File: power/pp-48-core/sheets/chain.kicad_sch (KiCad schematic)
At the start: 1 part, among them J301 CHAIN OUT

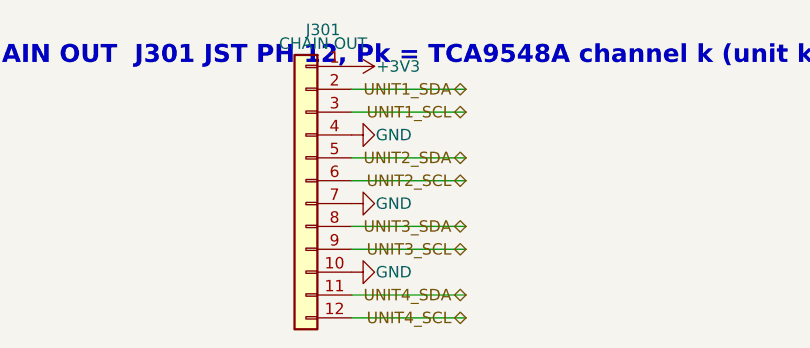
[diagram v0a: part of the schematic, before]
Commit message: pp-48 chained plane: unit board 76 x 72 (9 mm left margin for chain IN J301 + holes, user; slots as rev1 at x 100 / 125; 17 mm input strip with XT60, unit hot-swap, chain OUT J302) and core board 56 x 72 (rev1 core minus the tile, 8 mm right margin for chain OUT J301 + holes, mux U6 by the header, XT30 at the bottom) placed as drafts by tools/place_unit.py / place_core.py (boardfit.py helpers); chain headers on B, pins at v 39..61 on every board; pinout swapped so IN pin 1 = 3V3 / P0 at the bottom on B (flat cable n -> 13 - n); DRC 0 errors besides unconnected, parity clean; not routed; handoff
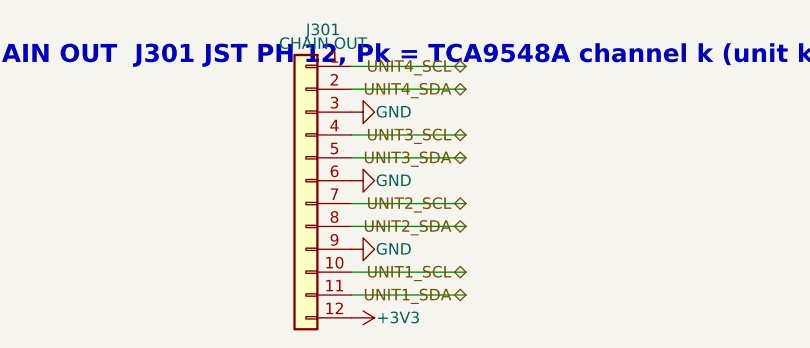
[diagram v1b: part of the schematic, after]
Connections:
- net +3V3: now also J301.12 (Pin_12); no longer J301.1 (Pin_1)
- net GND: now also J301.3 (Pin_3), J301.6 (Pin_6), J301.9 (Pin_9); no longer J301.10 (Pin_10), J301.4 (Pin_4), J301.7 (Pin_7)
- net UNIT1_SCL: now also J301.10 (Pin_10); no longer J301.3 (Pin_3)
- net UNIT1_SDA: now also J301.11 (Pin_11); no longer J301.2 (Pin_2)
- net UNIT2_SCL: now also J301.7 (Pin_7); no longer J301.6 (Pin_6)
- net UNIT2_SDA: now also J301.8 (Pin_8); no longer J301.5 (Pin_5)
- net UNIT3_SCL: now also J301.4 (Pin_4); no longer J301.9 (Pin_9)
- net UNIT3_SDA: now also J301.5 (Pin_5); no longer J301.8 (Pin_8)
- net UNIT4_SCL: now also J301.1 (Pin_1); no longer J301.12 (Pin_12)
- net UNIT4_SDA: now also J301.2 (Pin_2); no longer J301.11 (Pin_11)
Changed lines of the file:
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@@
+	(wire
+		(pts
+			(xy 81.28 38.1) (xy 93.98 38.1)
+		)
+		(stroke
+			(width 0)
+			(type default)
+		)
+	)
 	(wire
 		(pts
@@
 	(wire
 		(pts
-			(xy 81.28 43.18) (xy 93.98 43.18)
+			(xy 81.28 45.72) (xy 93.98 45.72)
 		)
 		(stroke
@@
 	(wire
 		(pts
-			(xy 81.28 50.8) (xy 93.98 50.8)
+			(xy 81.28 53.34) (xy 93.98 53.34)
 		)
 		(stroke
@@
 	(wire
 		(pts
-			(xy 81.28 58.42) (xy 93.98 58.42)
+			(xy 81.28 60.96) (xy 93.98 60.96)
 		)
 		(stroke
@@
 		)
 	)
-	(wire
-		(pts
-			(xy 81.28 66.04) (xy 93.98 66.04)
-		)
-		(stroke
-			(width 0)
-			(type default)
+	(hierarchical_label "UNIT4_SCL"
+		(shape bidirectional)
+		(at 93.98 38.1 180)
+		(effects
+			(font
+				(size 1.27 1.27)
+			)
+			(justify right)
+		)
+	)
+	(hierarchical_label "UNIT4_SDA"
+		(shape bidirectional)
+		(at 93.98 40.64 180)
+		(effects
+			(font
+				(size 1.27 1.27)
+			)
+			(justify right)
+		)
+	)
+	(hierarchical_label "UNIT3_SCL"
+		(shape bidirectional)
+		(at 93.98 45.72 180)
+		(effects
+			(font
+				(size 1.27 1.27)
+			)
+			(justify right)
+		)
+	)
+	(hierarchical_label "UNIT3_SDA"
+		(shape bidirectional)
+		(at 93.98 48.26 180)
+		(effects
+			(font
+				(size 1.27 1.27)
+			)
+			(justify right)
+		)
+	)
+	(hierarchical_label "UNIT2_SCL"
+		(shape bidirectional)
+		(at 93.98 53.34 180)
+		(effects
+			(font
+				(size 1.27 1.27)
+			)
+			(justify right)
+		)
+	)
+	(hierarchical_label "UNIT2_SDA"
+		(shape bidirectional)
+		(at 93.98 55.88 180)
+		(effects
+			(font
+				(size 1.27 1.27)
+			)
+			(justify right)
+		)
+	)
+	(hierarchical_label "UNIT1_SCL"
+		(shape bidirectional)
+		(at 93.98 60.96 180)
+		(effects
+			(font
+				(size 1.27 1.27)
+			)
+			(justify right)
 		)
 	)
 	(hierarchical_label "UNIT1_SDA"
 		(shape bidirectional)
-		(at 93.98 40.64 180)
-		(effects
-			(font
-				(size 1.27 1.27)
-			)
-			(justify right)
-		)
-	)
-	(hierarchical_label "UNIT1_SCL"
-		(shape bidirectional)
-		(at 93.98 43.18 180)
-		(effects
-			(font
-				(size 1.27 1.27)
-			)
-			(justify right)
-		)
-	)
-	(hierarchical_label "UNIT2_SDA"
-		(shape bidirectional)
-		(at 93.98 48.26 180)
-		(effects
-			(font
-				(size 1.27 1.27)
-			)
-			(justify right)
-		)
-	)
-	(hierarchical_label "UNIT2_SCL"
-		(shape bidirectional)
-		(at 93.98 50.8 180)
-		(effects
-			(font
-				(size 1.27 1.27)
-			)
-			(justify right)
-		)
-	)
-	(hierarchical_label "UNIT3_SDA"
-		(shape bidirectional)
-		(at 93.98 55.88 180)
-		(effects
-			(font
-				(size 1.27 1.27)
-			)
-			(justify right)
-		)
-	)
-	(hierarchical_label "UNIT3_SCL"
-		(shape bidirectional)
-		(at 93.98 58.42 180)
-		(effects
-			(font
-				(size 1.27 1.27)
-			)
-			(justify right)
-		)
-	)
-	(hierarchical_label "UNIT4_SDA"
-		(shape bidirectional)
 		(at 93.98 63.5 180)
-		(effects
-			(font
-				(size 1.27 1.27)
-			)
-			(justify right)
-		)
-	)
-	(hierarchical_label "UNIT4_SCL"
-		(shape bidirectional)
-		(at 93.98 66.04 180)
 		(effects
 			(font
@@
 	)
 	(symbol
-		(lib_id "power:+3V3")
-		(at 81.28 38.1 270)
+		(lib_id "power:GND")
+		(at 81.28 43.18 90)
 		(unit 1)
 		(body_style 1)
@@
 		(dnp no)
 		(property "Reference" "#PWR8001"
-			(at 81.28 38.1 90)
-			(hide yes)
-			(show_name no)
-			(do_not_autoplace no)
-			(effects
-				(font
-					(size 1.27 1.27)
-				)
-			)
-		)
-		(property "Value" "+3V3"
-			(at 86.455 38.1 90)
+			(at 81.28 43.18 90)
+			(hide yes)
+			(show_name no)
+			(do_not_autoplace no)
+			(effects
+				(font
+					(size 1.27 1.27)
+				)
+			)
+		)
+		(property "Value" "GND"
+			(at 85.955 43.18 90)
 			(show_name no)
 			(do_not_autoplace no)
@@
 		)
 		(property "Footprint" ""
-			(at 81.28 38.1 0)
+			(at 81.28 43.18 0)
 			(hide yes)
 			(show_name no)
@@
 		)
 		(property "Datasheet" ""
-			(at 81.28 38.1 0)
+			(at 81.28 43.18 0)
 			(hide yes)
 			(show_name no)
@@
 		)
 		(property "Description" ""
-			(at 81.28 38.1 0)
+			(at 81.28 43.18 0)
 			(hide yes)
 			(show_name no)
@@
 	(symbol
 		(lib_id "power:GND")
-		(at 81.28 45.72 90)
+		(at 81.28 50.8 90)
 		(unit 1)
 		(body_style 1)
@@
 		(dnp no)
 		(property "Reference" "#PWR8002"
-			(at 81.28 45.72 90)
+			(at 81.28 50.8 90)
 			(hide yes)
 			(show_name no)
@@
 		)
 		(property "Value" "GND"
-			(at 85.955 45.72 90)
+			(at 85.955 50.8 90)
 			(show_name no)
 			(do_not_autoplace no)
@@
 		)
 		(property "Footprint" ""
-			(at 81.28 45.72 0)
+			(at 81.28 50.8 0)
 			(hide yes)
 			(show_name no)
@@
 		)
 		(property "Datasheet" ""
-			(at 81.28 45.72 0)
+			(at 81.28 50.8 0)
 			(hide yes)
 			(show_name no)
@@
 		)
 		(property "Description" ""
-			(at 81.28 45.72 0)
+			(at 81.28 50.8 0)
 			(hide yes)
 			(show_name no)
@@
 	(symbol
 		(lib_id "power:GND")
-		(at 81.28 53.34 90)
+		(at 81.28 58.42 90)
 		(unit 1)
 		(body_style 1)
@@
 		(dnp no)
 		(property "Reference" "#PWR8003"
-			(at 81.28 53.34 90)
+			(at 81.28 58.42 90)
 			(hide yes)
 			(show_name no)
@@
 		)
 		(property "Value" "GND"
-			(at 85.955 53.34 90)
+			(at 85.955 58.42 90)
 			(show_name no)
 			(do_not_autoplace no)
@@
 		)
 		(property "Footprint" ""
-			(at 81.28 53.34 0)
+			(at 81.28 58.42 0)
 			(hide yes)
 			(show_name no)
@@
 		)
 		(property "Datasheet" ""
-			(at 81.28 53.34 0)
+			(at 81.28 58.42 0)
 			(hide yes)
 			(show_name no)
@@
 		)
 		(property "Description" ""
-			(at 81.28 53.34 0)
+			(at 81.28 58.42 0)
 			(hide yes)
 			(show_name no)
@@
 	)
 	(symbol
-		(lib_id "power:GND")
-		(at 81.28 60.96 90)
+		(lib_id "power:+3V3")
+		(at 81.28 66.04 270)
 		(unit 1)
 		(body_style 1)
@@
 		(dnp no)
 		(property "Reference" "#PWR8004"
-			(at 81.28 60.96 90)
-			(hide yes)
-			(show_name no)
-			(do_not_autoplace no)
-			(effects
-				(font
-					(size 1.27 1.27)
-				)
-			)
-		)
-		(property "Value" "GND"
-			(at 85.955 60.96 90)
+			(at 81.28 66.04 90)
+			(hide yes)
+			(show_name no)
+			(do_not_autoplace no)
+			(effects
+				(font
+					(size 1.27 1.27)
+				)
+			)
+		)
+		(property "Value" "+3V3"
+			(at 86.455 66.04 90)
 			(show_name no)
 			(do_not_autoplace no)
@@
 		)
 		(property "Footprint" ""
-			(at 81.28 60.96 0)
+			(at 81.28 66.04 0)
 			(hide yes)
 			(show_name no)
@@
 		)
 		(property "Datasheet" ""
-			(at 81.28 60.96 0)
+			(at 81.28 66.04 0)
 			(hide yes)
 			(show_name no)
@@
 		)
 		(property "Description" ""
-			(at 81.28 60.96 0)
-			(hide yes)
-			(show_name no)
+			(at 81.28 66.04 0)
+			(hide yes)
+			(show_name no)

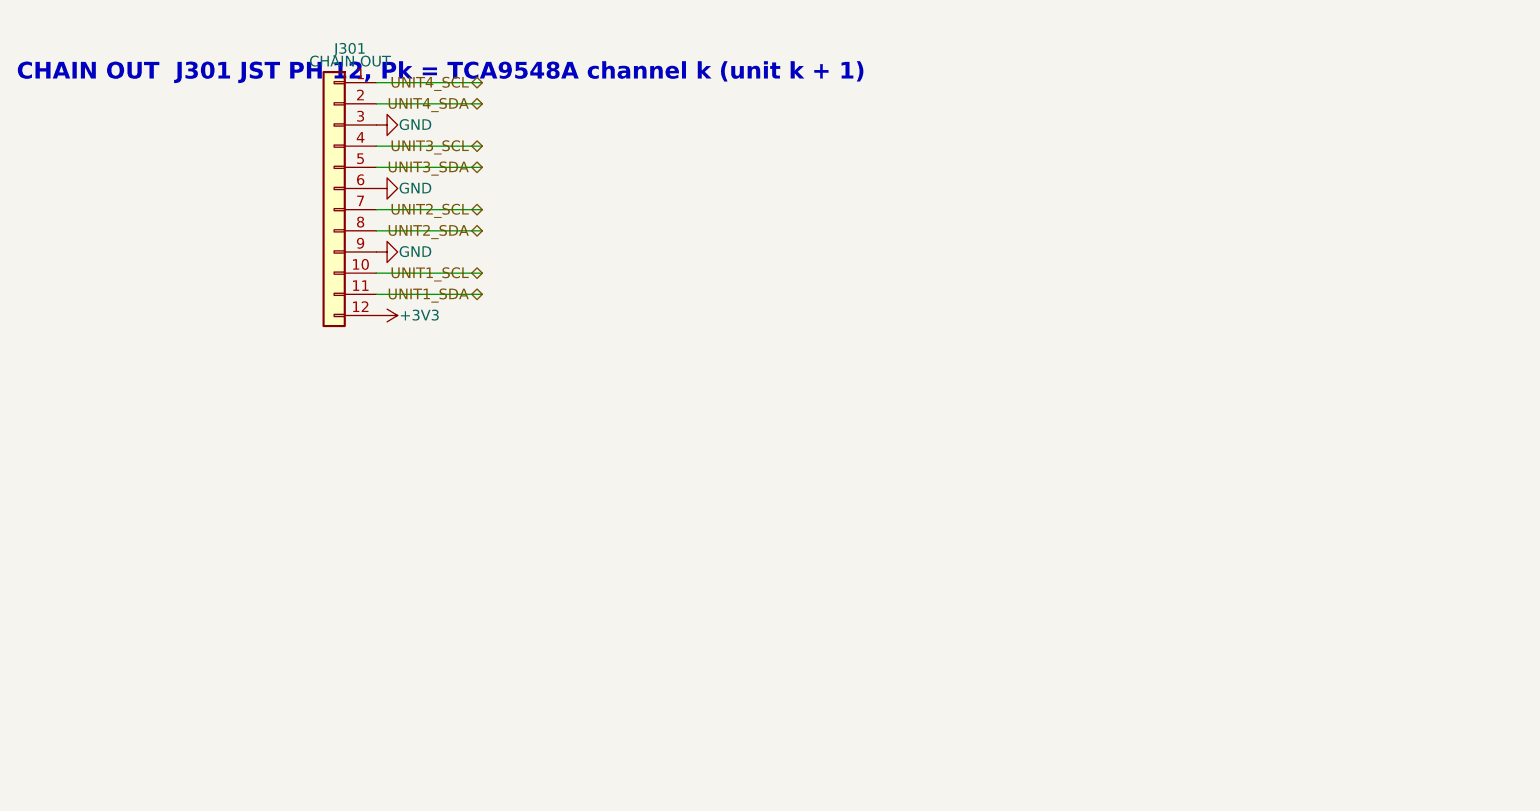
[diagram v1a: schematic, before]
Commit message: pp-48 plane boards: press deadline line (docs/press-deadline-line.md decided: option B + A) on a 14-pin chain (S14B-PH-K-S C157938; 13 PRESS_EN, 14 EXP_RSTN, cable n -> 15 - n, pins v 35..61); unit Q10 / R31 switch the photoMOS LED returns (PRESS_RTN), core U301 74LVC1G123 deadline (pp:74LVC1G123 single-unit copy) on PC6 PRESS_TRIG, PC7 EXP_RSTN to the units' /RESET; ERC 0 both; boards rebuilt and placed, unit 78.5 x 72 with the strip power path re-placed top-down; unit routing tools (route_unit.py hand copper + In2 band / +3V3 trunk, unitsplit.py, route_unit.sh flow): DRC 0 errors, ~10 unconnected at expander U5; core placed, not routed; pmmount.py restored from granite_controller; ADR 0005 decision 4; handoff
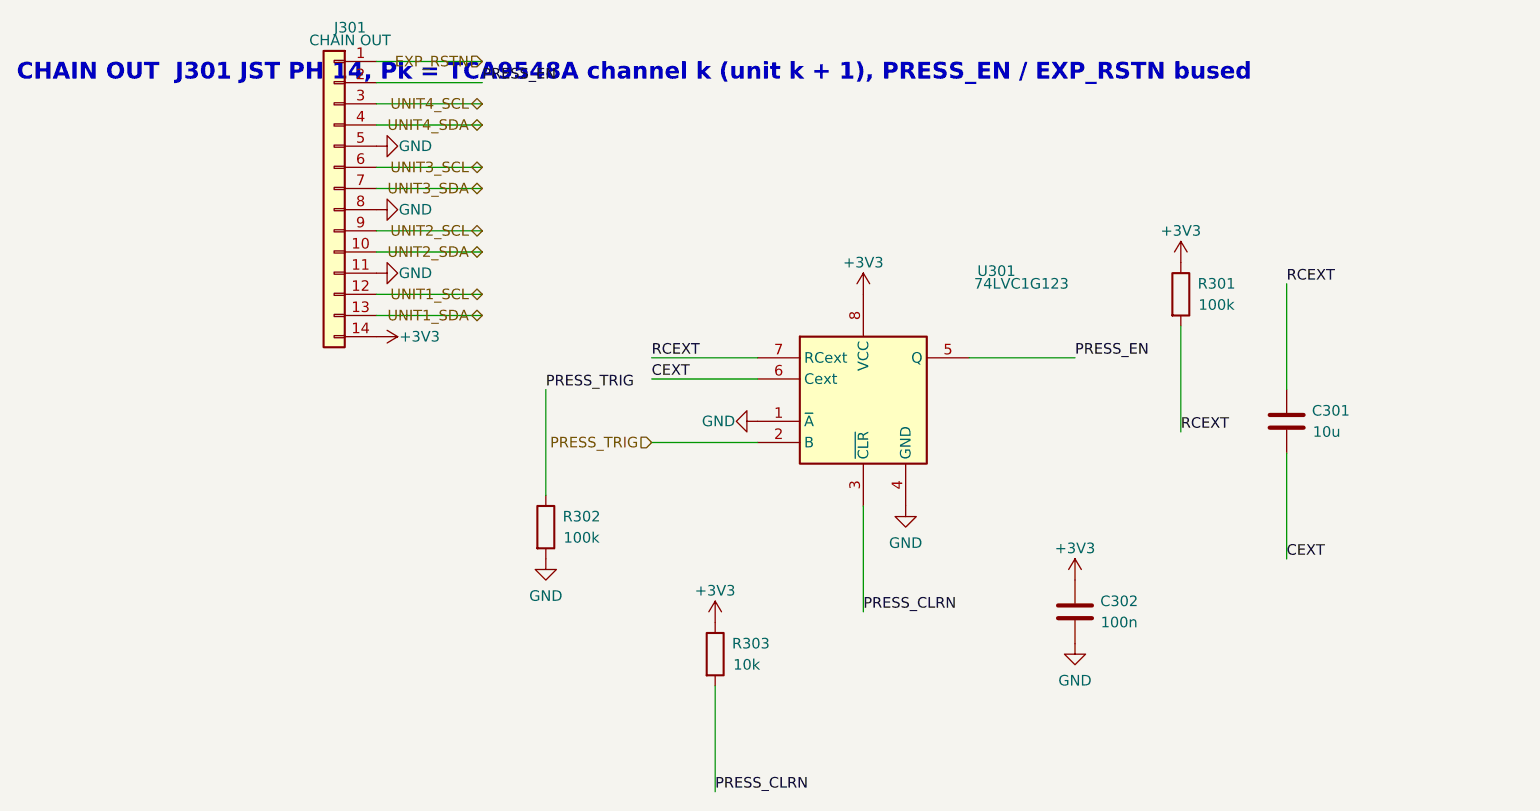
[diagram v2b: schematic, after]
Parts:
- added C301: 10u, Capacitor_SMD:C_0805_2012Metric, symbol Device:C
- added C302: 100n, Capacitor_SMD:C_0402_1005Metric, symbol Device:C
- added R301, R302: 100k, Resistor_SMD:R_0402_1005Metric, symbol Device:R
- added R303: 10k, Resistor_SMD:R_0402_1005Metric, symbol Device:R
- added U301: 74LVC1G123, Package_SO:SSOP-8_2.95x2.8mm_P0.65mm, symbol pp:74LVC1G123
- J301: footprint Connector_JST:JST_PH_S12B-PH-K_1x12_P2.00mm_Horizontal -> Connector_JST:JST_PH_S14B-PH-K_1x14_P2.00mm_Horizontal; symbol Connector_Generic:Conn_01x12 -> Connector_Generic:Conn_01x14; LCSC C157943 -> C157938; MPN JST S12B-PH-K-S(LF)(SN) -> JST S14B-PH-K-S(LF)(SN)
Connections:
- net +3V3: now also J301.14 (Pin_14), C302.1, R301.1, R303.1, U301.8 (VCC); no longer J301.12 (Pin_12)
- net GND: now also J301.11 (Pin_11), J301.5 (Pin_5), J301.8 (Pin_8), C302.2, R302.2, U301.1 (~{A}), U301.4 (GND); no longer J301.3 (Pin_3), J301.6 (Pin_6), J301.9 (Pin_9)
- net UNIT1_SCL: now also J301.12 (Pin_12); no longer J301.10 (Pin_10)
- net UNIT1_SDA: now also J301.13 (Pin_13); no longer J301.11 (Pin_11)
- net UNIT2_SCL: now also J301.9 (Pin_9); no longer J301.7 (Pin_7)
- net UNIT2_SDA: now also J301.10 (Pin_10); no longer J301.8 (Pin_8)
- net UNIT3_SCL: now also J301.6 (Pin_6); no longer J301.4 (Pin_4)
- net UNIT3_SDA: now also J301.7 (Pin_7); no longer J301.5 (Pin_5)
- net UNIT4_SCL: now also J301.3 (Pin_3); no longer J301.1 (Pin_1)
- net UNIT4_SDA: now also J301.4 (Pin_4); no longer J301.2 (Pin_2)
- new net CEXT: C301.2, U301.6 (Cext)
- new net EXP_RSTN: J301.1 (Pin_1)
- new net PRESS_CLRN: R303.2, U301.3 (~{CLR})
- new net PRESS_EN: J301.2 (Pin_2), U301.5 (Q)
- new net PRESS_TRIG: R302.1, U301.2 (B)
- new net RCEXT: C301.1, R301.2, U301.7 (RCext)
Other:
- note added: "CHAIN OUT J301 JST PH 14, Pk = TCA9548A channel k (unit k + 1), PRESS_EN / EXP_RSTN bused"
- note removed: "CHAIN OUT J301 JST PH 12, Pk = TCA9548A channel k (unit k + 1)"
